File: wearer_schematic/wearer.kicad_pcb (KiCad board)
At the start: 2 copper layers, 43 parts, among them J1 Conn_01x02_Male, J2 Conn_01x06, Q1 AO3400A, SW1 SW_SPST, SW2 SW_Push, SW3 SW_Push, SW4 SW_Push, U1 MQ-9B, U2 74HC14, U3 ESP32-WROOM-32D, U4 LSM6DSLTR, U5 SEN-11574, U6 RFM9-LoRa-Radio

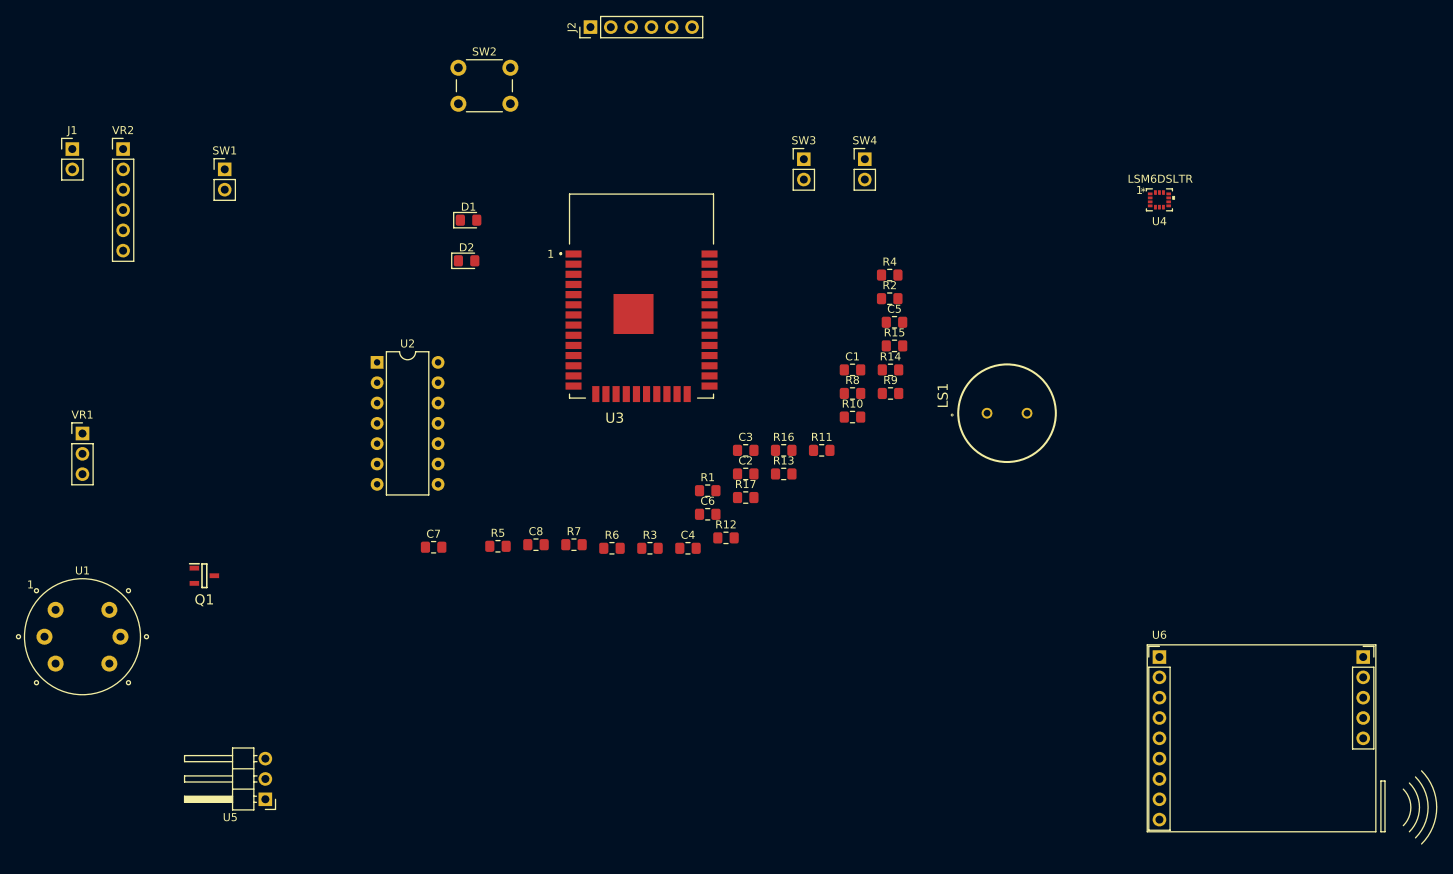
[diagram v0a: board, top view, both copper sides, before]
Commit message: arranging components
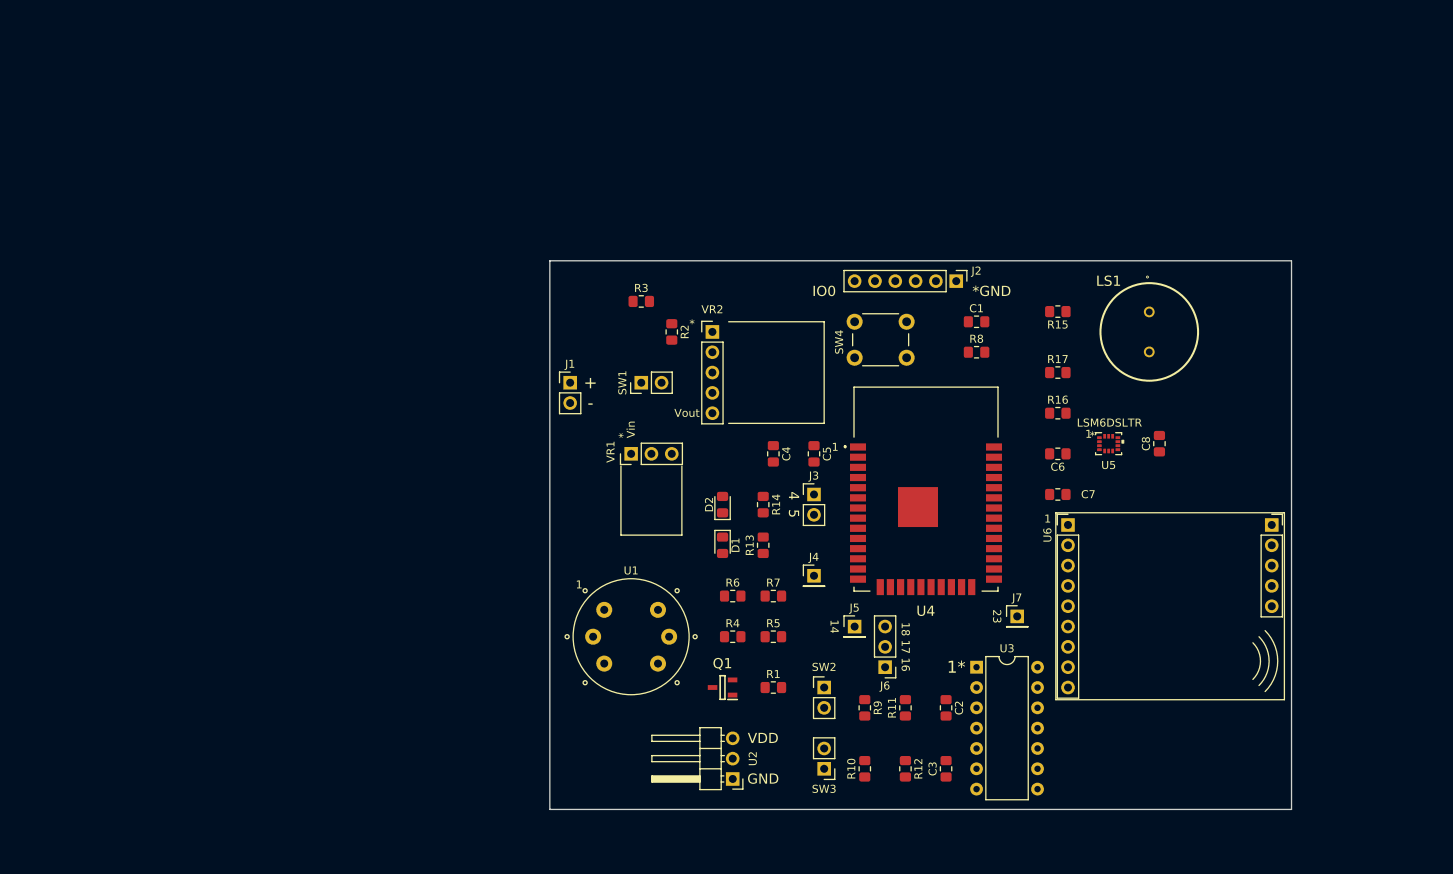
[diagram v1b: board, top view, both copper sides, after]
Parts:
- added J3: P4:5, Connector_PinHeader_2.54mm:PinHeader_1x02_P2.54mm_Vertical, F.Cu at (160.0, 87.6)
- added J4: P7, Connector_PinHeader_2.54mm:PinHeader_1x01_P2.54mm_Vertical, F.Cu at (160.0, 97.8)
- added J5: P14, Connector_PinHeader_2.54mm:PinHeader_1x01_P2.54mm_Vertical, F.Cu at (165.1, 104.1)
- added J6: P16:18, Connector_PinHeader_2.54mm:PinHeader_1x03_P2.54mm_Vertical, F.Cu at (168.9, 109.2)
- added J7: P23, Connector_PinHeader_2.54mm:PinHeader_1x01_P2.54mm_Vertical, F.Cu at (185.4, 102.9)
- R12: value 68 -> 10k
- R13, R14: value 10k -> 68
- R15: value 68 -> 1K
- R7: value 2900 -> 3000
- R8: value 1K -> 10k
- SW2: footprint Button_Switch_THT:SW_PUSH_6mm -> Connector_PinHeader_2.54mm:PinHeader_1x02_P2.54mm_Vertical
- SW4: footprint Connector_PinHeader_2.54mm:PinHeader_1x02_P2.54mm_Vertical -> Button_Switch_THT:SW_PUSH_6mm
- U2: value 74HC14 -> SEN-11574; footprint Package_DIP:DIP-14_W7.62mm -> Connector_PinHeader_2.54mm:PinHeader_1x03_P2.54mm_Horizontal
- U3: value ESP32-WROOM-32D -> 74HC14; footprint noggin:ESP32WROOM32D -> Package_DIP:DIP-14_W7.62mm
- U4: value LSM6DSLTR -> ESP32-WROOM-32D; footprint noggin:LSM6DSLTR -> noggin:ESP32WROOM32D
- U5: value SEN-11574 -> LSM6DSLTR; footprint Connector_PinHeader_2.54mm:PinHeader_1x03_P2.54mm_Horizontal -> noggin:LSM6DSLTR
- VR1: footprint Connector_PinHeader_2.54mm:PinHeader_1x03_P2.54mm_Vertical -> noggin:U1V10F5-VR
- VR2: footprint Connector_PinHeader_2.54mm:PinHeader_1x06_P2.54mm_Vertical -> noggin:S9V11F3S5C3
- moved U5 114.4 mm to (196.8, 81.3), turned to 0 degrees
- moved SW2 90.0 mm to (161.3, 111.8)
- moved C8 79.0 mm to (203.2, 81.3), turned to 90 degrees
- moved C7 78.3 mm to (190.5, 87.6), turned to 180 degrees
- moved VR2 77.1 mm to (147.3, 67.3)
- moved SW3 76.2 mm to (161.3, 121.9), turned to 180 degrees
- moved J1 68.7 mm to (129.5, 73.7)
- moved VR1 68.6 mm to (137.2, 82.5), turned to 90 degrees
- moved U1 68.6 mm to (137.2, 105.4)
- moved U2 68.5 mm to (149.9, 123.2), turned to 180 degrees
- moved Q1 66.3 mm to (148.6, 111.8), turned to 180 degrees
- moved U3 62.5 mm to (180.3, 109.2)
- moved SW1 58.5 mm to (138.4, 73.7), turned to 90 degrees
- moved J2 55.7 mm to (177.8, 61.0), turned to 270 degrees
- moved D1 51.6 mm to (148.6, 94.0), turned to 270 degrees
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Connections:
- R1 pad 2: GPIO25 -> GPIO25_GAS
- R11 pad 1: +3V3 -> Net-(R11-Pad1)
- R11 pad 2: Net-(R11-Pad2) -> Net-(C2-Pad1)
- R12 pad 1: Net-(D1-Pad2) -> Net-(R10-Pad2)
- R12 pad 2: GPIO14 -> Net-(C3-Pad1)
- R13 pad 1: Net-(R10-Pad2) -> Net-(D1-Pad2)
- R13 pad 2: Net-(C2-Pad1) -> GPIO14_LED
- R14 pad 1: Net-(R11-Pad2) -> Net-(D2-Pad2)
- R14 pad 2: Net-(C3-Pad1) -> GPIO27_LED
- R15 pad 1: Net-(D2-Pad2) -> Net-(LS1-Pad1)
- R15 pad 2: GPIO27 -> GPIO26_BUZZ
- R2 pad 1: ADC1_CH6 -> ADC1_CH6_BAT
- R3 pad 2: ADC1_CH6 -> ADC1_CH6_BAT
- R6 pad 2: ADC1_CH5 -> ADC1_CH5_GAS
- R7 pad 1: ADC1_CH5 -> ADC1_CH5_GAS
- R8 pad 1: Net-(LS1-Pad1) -> EN
- R8 pad 2: GPIO26 -> +3V3
- R9 pad 1: EN -> +3V3
- R9 pad 2: +3V3 -> Net-(R11-Pad1)
- SW2 pad 2: EN -> Net-(R11-Pad1)
- SW4 pad 2: Net-(R11-Pad2) -> EN
- U2 pad 1: Net-(C2-Pad1) -> GND
- U2 pad 2: GPIO5 -> ADC1_CH4_PULSE
- U2 pad 3: Net-(C3-Pad1) -> +3V3
- U3 pad 1: GND -> Net-(C2-Pad1)
- U3 pad 10: GPIO25 -> Net-(U3-Pad10)
- U3 pad 11: GPIO26 -> GND
- U3 pad 12: GPIO27 -> Net-(U3-Pad12)
- U3 pad 13: GPIO14 -> GND
- U3 pad 14: Net-(U3-Pad14) -> +3V3
- U3 pad 2: +3V3 -> GPIO5_SW
- U3 pad 3: EN -> Net-(C3-Pad1)
- U3 pad 4: Net-(U3-Pad4) -> GPIO17_SW
- U3 pad 5: Net-(U3-Pad5) -> GND
- U3 pad 6: ADC1_CH6 -> Net-(U3-Pad6)
- U3 pad 7: Net-(U3-Pad7) -> GND
- U3 pad 8: ADC1_CH4 -> Net-(U3-Pad8)
- U3 pad 9: ADC1_CH5 -> GND
- U4 pad 1: SDO -> GND
- U4 pad 10: Net-(U4-Pad10) -> GPIO25_GAS
- U4 pad 11: Net-(U4-Pad11) -> GPIO26_BUZZ
- U4 pad 12: Net-(C6-Pad1) -> GPIO27_LED
- U4 pad 13: SCL -> GPIO14_LED
- U4 pad 14: SDA -> P14
- U4 pad 2: GND -> +3V3
- U4 pad 3: GND -> EN
- U4 pad 4: GPIO18 -> P4
- U4 pad 5: Net-(C6-Pad1) -> P5
- U4 pad 6: GND -> ADC1_CH6_BAT
- U4 pad 7: GND -> P7
- U4 pad 8: +3V3 -> ADC1_CH4_PULSE
- U4 pad 9: GPIO19 -> ADC1_CH5_GAS
- U5 pad 1: GND -> SDO
- U5 pad 2: ADC1_CH4 -> GND
- U5 pad 3: +3V3 -> GND
- U6 pad 3: GPIO2 -> GPIO2_LORA
- U6 pad 4: GPIO4 -> GPIO4_LORA
- U6 pad 9: GPIO16 -> GPIO16_LORA
- VR2 pad 1: +3V3 -> Net-(VR2-Pad1)
- VR2 pad 2: GND -> Net-(VR2-Pad2)
- VR2 pad 4: Net-(VR2-Pad4) -> GND
- VR2 pad 5: Net-(VR2-Pad5) -> +3V3
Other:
- board outline added: 92.7 x 68.6 mm
- net class Default: clearance 0.2 -> 0.2032; trace_width 0.25 -> 0.2032; via_dia 0.8 -> 0.6858; via_drill 0.4 -> 0.3302
- rule trace_clearance: 0.2 -> 0.2032
- rule trace_min: 0.1524 -> 0.2032
- rule via_min_drill: 0.254 -> 0.3302
- rule via_min_size: 0.508 -> 0.6858
- board text added: "*GND"
- board text added: "+"
- board text added: "-"
- board text added: "1*"
- board text added: "14"
- board text added: "18 17 16"
- board text added: "23"
- board text added: "4 5"
- board text added: "GND"
- board text added: "IO0"
- board text added: "VDD"

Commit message: before adding decoupling to power
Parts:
- moved J4 2.62 mm to (160.7, 95.2)
- moved U3 1.91 mm to (180.3, 107.3)
- moved U1 1.80 mm to (135.9, 104.1)
- moved R4 1.42 mm to (149.2, 104.1)
- moved R6 1.42 mm to (149.2, 99.1)
- moved J3 1.42 mm to (160.7, 86.4)
- moved R5 1.42 mm to (154.3, 104.1)
- moved R7 1.42 mm to (154.3, 99.1)
- moved C1 1.27 mm to (180.3, 64.8)
- moved D1 1.27 mm to (148.6, 92.7)
- moved D2 1.27 mm to (148.6, 87.6)
- moved J7 1.27 mm to (185.4, 101.6)
- moved Q1 1.27 mm to (148.6, 110.5)
- moved R1 1.27 mm to (154.9, 110.5)
- moved R13 1.27 mm to (153.7, 92.7)
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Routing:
- net +3V3: track 0.00 -> 244.4 mm
- net +5V: track 0.00 -> 38.7 mm
- net Net-(R2-Pad2): track 0.00 -> 13.1 mm
- net Net-(J1-Pad1): track 0.00 -> 8.89 mm
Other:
- board size 92.7 x 68.6 mm -> 92.7 x 69.8 mm
- board text added: "5V"

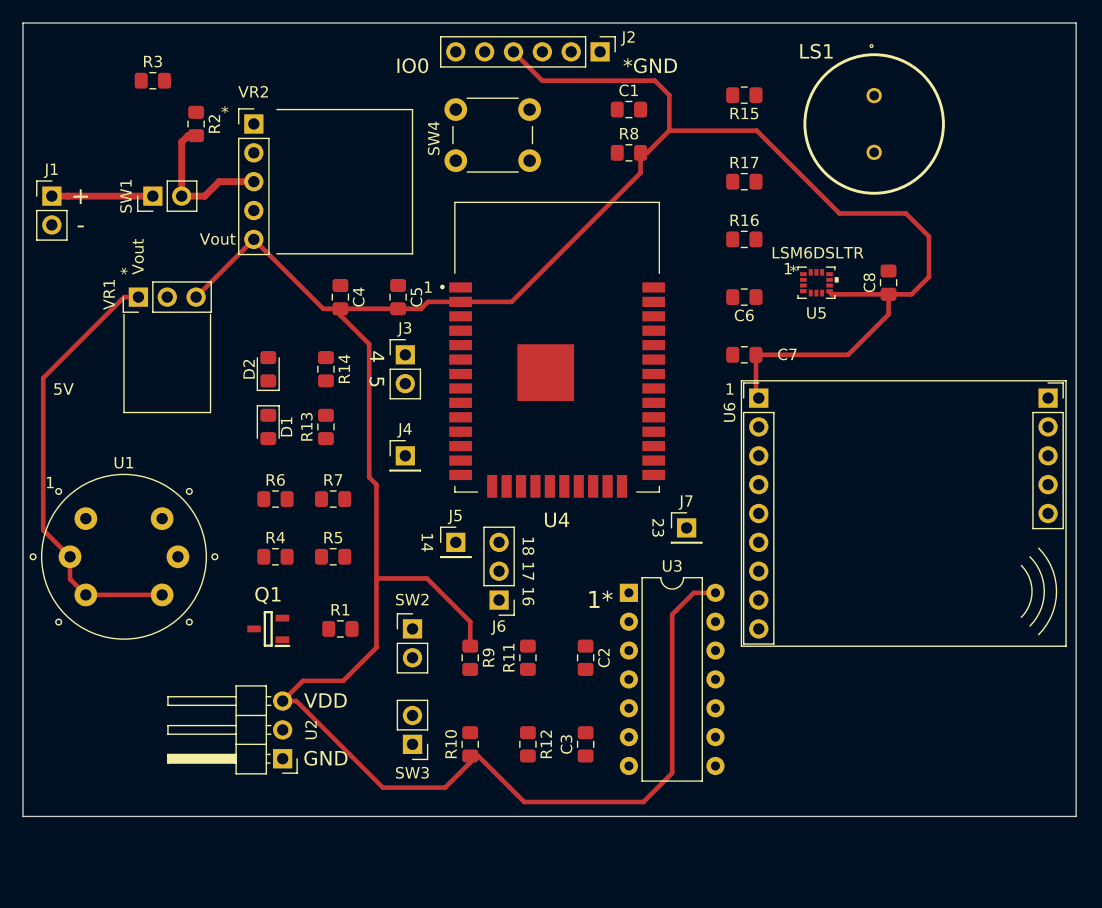
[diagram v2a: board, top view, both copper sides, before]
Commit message: everything but ground plane
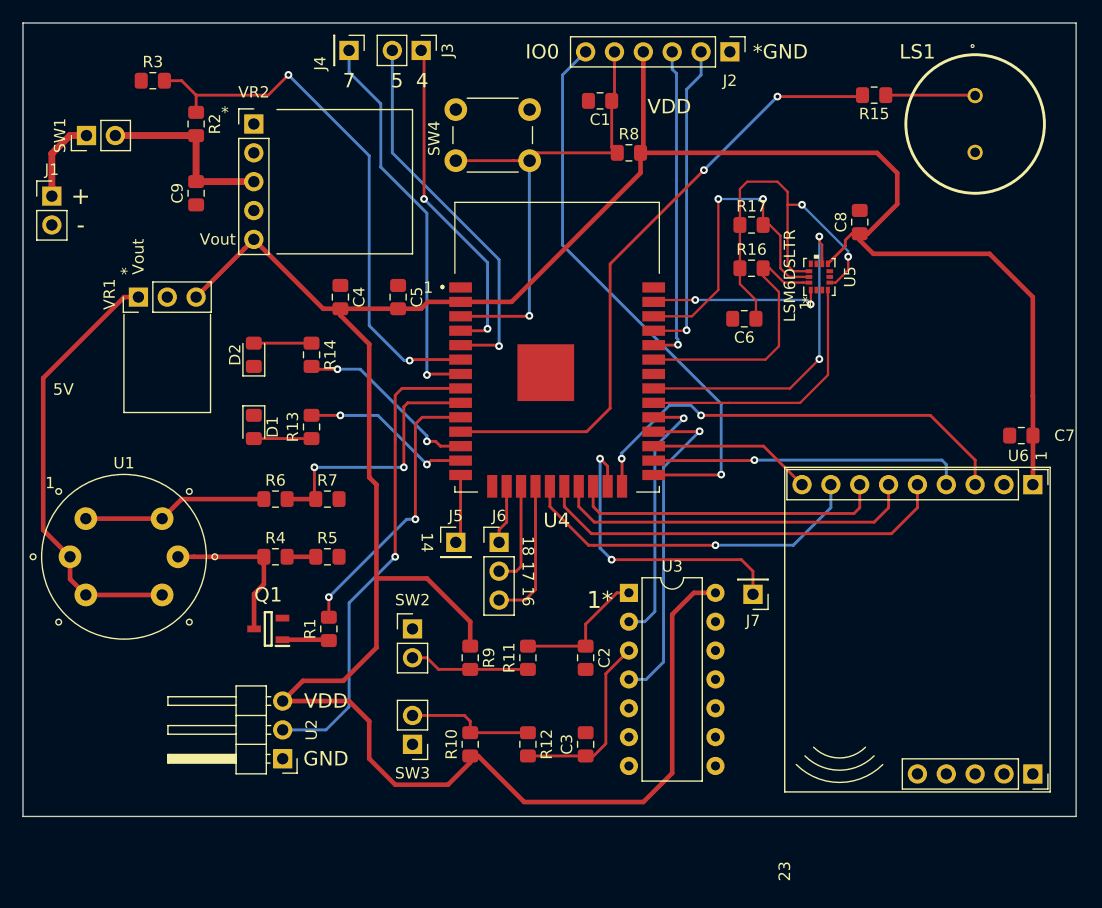
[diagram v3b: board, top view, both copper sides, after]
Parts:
- added C9: 33uF, Capacitor_SMD:C_0805_2012Metric_Pad1.15x1.40mm_HandSolder, F.Cu at (142.2, 72.1)
- moved J4 36.0 mm to (155.7, 59.6), turned to 270 degrees
- moved J3 26.8 mm to (162.1, 59.6), turned to 270 degrees
- moved C7 25.4 mm to (214.9, 93.5)
- moved U6 25.3 mm to (215.9, 97.8), turned to 270 degrees
- moved R15 11.4 mm to (201.9, 63.5)
- moved J2 11.4 mm to (189.2, 59.7)
- moved LS1 8.89 mm to (210.8, 66.0)
- moved J7 8.26 mm to (191.3, 107.4), turned to 180 degrees
- moved SW1 7.91 mm to (132.6, 67.1)
- moved C8 5.91 mm to (200.7, 74.7)
- moved J6 5.08 mm to (168.9, 102.9), turned to 0 degrees
- moved R17 3.86 mm to (191.1, 74.9)
- moved C1 2.65 mm to (177.8, 64.0), turned to 180 degrees
- moved R16 2.62 mm to (191.1, 78.7)
- moved C6 1.91 mm to (190.5, 83.2)
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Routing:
- net GPIO26_BUZZ: track 0.00 -> 55.1 mm, vias 0 -> 2
- net GPIO0: track 0.00 -> 49.8 mm, vias 0 -> 1
- net ADC1_CH6_BAT: track 0.00 -> 48.1 mm, vias 0 -> 2
- net EN: track 0.00 -> 43.4 mm, vias 0 -> 1
- net ADC1_CH4_PULSE: track 0.00 -> 41.8 mm, vias 0 -> 1
- net GPIO2_LORA: track 0.00 -> 40.0 mm, vias 0 -> 2
- net Net-(C6-Pad1): track 0.00 -> 36.9 mm, vias 0 -> 2
- net SPI_SCK: track 0.00 -> 36.8 mm
- net P7: track 0.00 -> 34.4 mm, vias 0 -> 1
- net P5: track 0.00 -> 33.4 mm, vias 0 -> 1
- net SPI_MISO: track 0.00 -> 32.2 mm
- net SPI_CS: track 0.00 -> 31.3 mm, vias 0 -> 1
- net P4: track 0.00 -> 29.4 mm, vias 0 -> 2
- net GPIO17_SW: track 0.00 -> 29.4 mm, vias 0 -> 1
- net GPIO19_ACC: track 0.00 -> 29.0 mm, vias 0 -> 2
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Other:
- board text added: "5 4"
- board text added: "7"
- board text removed: "4 5"
